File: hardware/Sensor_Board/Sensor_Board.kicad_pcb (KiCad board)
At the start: 2 copper layers, 83 x 83 mm, 55 parts, among them J1 Antenna, J2 Antenna, J3 Sensors, U1 ICM-42670-P, U10 PE42421, U12 SX1262IMLTRT, U2 SX1262IMLTRT, U3 0900FM15D0039, U4 BME280, U5 PE42421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

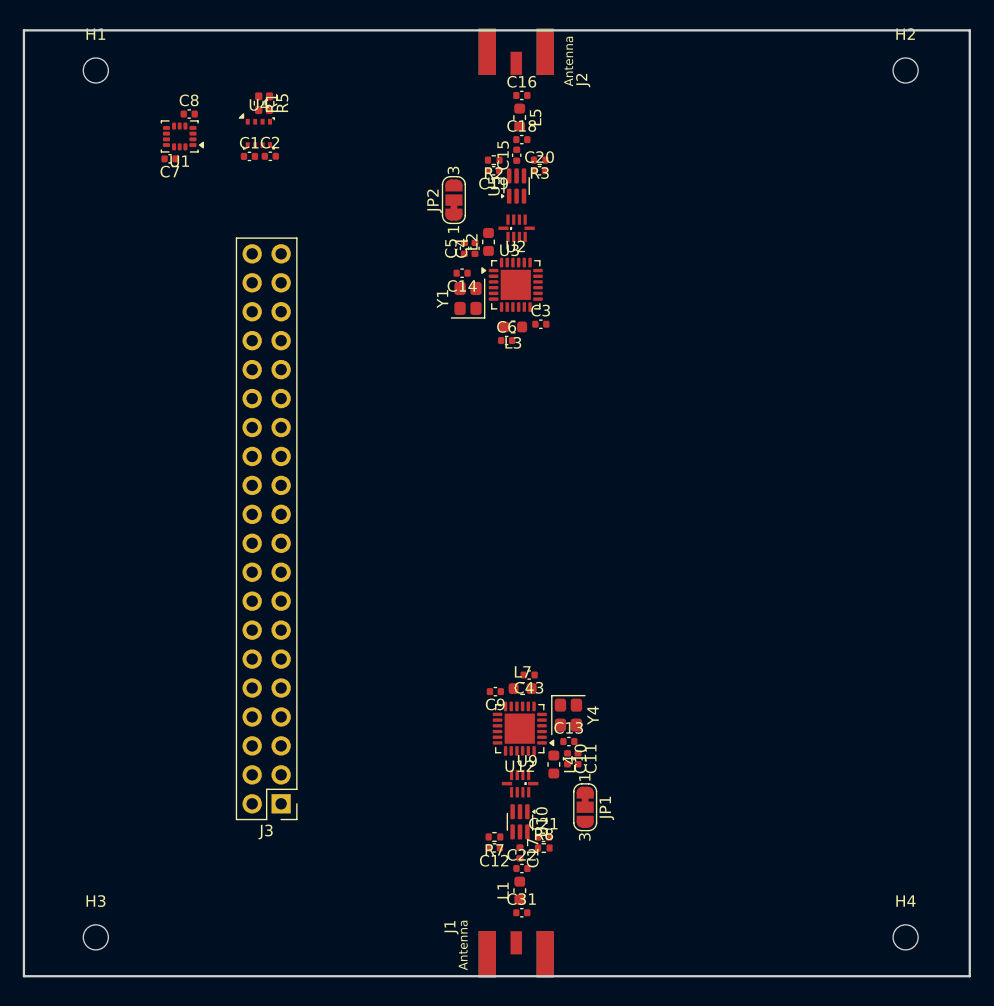
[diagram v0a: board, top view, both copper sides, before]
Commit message: feat(Hw):Update_Route_And_3d_Model_PWNsat_Batt_Board_And_Sensors
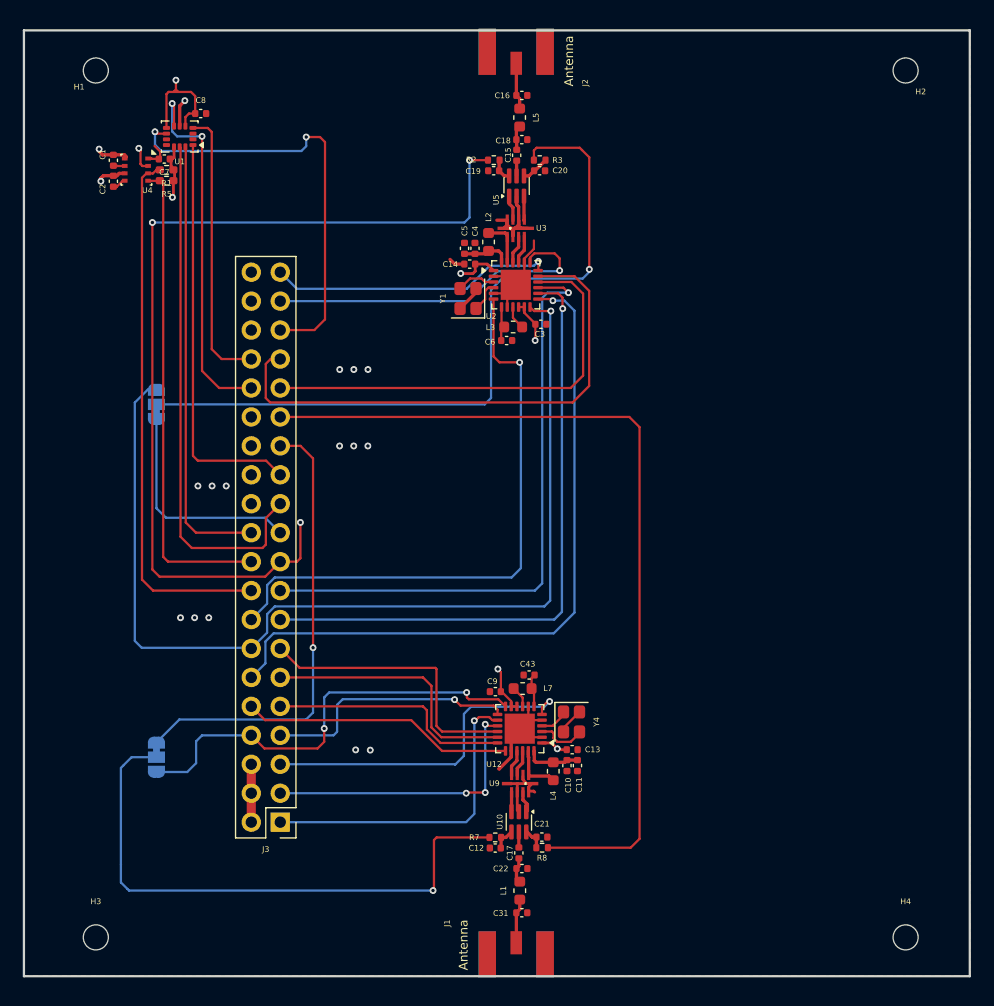
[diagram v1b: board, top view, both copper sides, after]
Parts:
- JP1, JP2: moved to B.Cu
- moved JP1 37.9 mm to (81.4, 122.4)
- moved JP2 31.7 mm to (81.4, 91.5)
- moved C2 13.9 mm to (77.7, 71.9), turned to -90 degrees
- moved C1 11.9 mm to (77.7, 70.1), turned to -90 degrees
- moved R5 11.3 mm to (82.3, 71.8), turned to 180 degrees
- moved U4 11.2 mm to (79.7, 70.9), turned to -90 degrees
- moved R1 9.98 mm to (82.3, 70.9), turned to 180 degrees
- moved J3 1.61 mm to (92.3, 128.1)
- moved C14 1.04 mm to (108.9, 79.2)
- moved C8 1.01 mm to (85.3, 66.0)
- moved C13 0.77 mm to (117.9, 121.8)
- moved Y4 0.66 mm to (117.8, 119.3)
- moved C10 0.60 mm to (117.5, 123.2)
- moved C11 0.60 mm to (118.4, 123.2)
- moved L4 0.60 mm to (116.2, 123.7)
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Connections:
- C13 pad 1: +3V3 -> +3.3V
- C14 pad 1: +3V3 -> +3.3V
- C3 pad 1: +3V3 -> +3.3V
- C9 pad 1: +3V3 -> +3.3V
- J3 pad 1: /Inputs_Connectors/DIO2 -> /Inputs_Connectors/R0_BUSY
- J3 pad 10: /Inputs_Connectors/SCL_ICM -> /Inputs_Connectors/R0_NSS
- J3 pad 11: /Inputs_Connectors/R0_RST -> /Inputs_Connectors/R0_MOSI
- J3 pad 12: /Inputs_Connectors/AP_ADO -> /Inputs_Connectors/R1_DIO1
- J3 pad 13: /Inputs_Connectors/R0_BUSY -> /Inputs_Connectors/R0_MISO
- J3 pad 14: /Inputs_Connectors/INT1 -> /Sensors/R1_DIO2
- J3 pad 15: /Inputs_Connectors/R0_DIO3 -> /Inputs_Connectors/R1_BUSY
- J3 pad 16: /Inputs_Connectors/FSYNC -> /Inputs_Connectors/R1_DIO3
- J3 pad 17: /Sensors/R0_DIO2 -> /Inputs_Connectors/R1_RST
- J3 pad 18: /Inputs_Connectors/INT2 -> /Inputs_Connectors/SDA_BME280
- J3 pad 19: /Inputs_Connectors/R0_DIO1 -> /Inputs_Connectors/R1_ANT_SW
- J3 pad 20: /Inputs_Connectors/SDA_BME280 -> /Inputs_Connectors/SCL_BME280
- J3 pad 21: /Inputs_Connectors/R0_ANT_SW -> /Inputs_Connectors/DIO23
- J3 pad 22: /Inputs_Connectors/SCL_BME280 -> /Inputs_Connectors/SDA_ICM
- J3 pad 23: /Inputs_Connectors/R1_ANT_SW -> /Inputs_Connectors/SCL_ICM
- J3 pad 25: /Inputs_Connectors/DIO23 -> /Inputs_Connectors/AP_ADO
- J3 pad 27: /Inputs_Connectors/R1_NSS -> /Inputs_Connectors/DIO2
- J3 pad 29: /Inputs_Connectors/R1_SCK -> /Inputs_Connectors/R0_ANT_SW
- J3 pad 3: /Inputs_Connectors/R0_NSS -> /Inputs_Connectors/R0_RST
- J3 pad 32: /Inputs_Connectors/R1_DIO1 -> /Inputs_Connectors/FSYNC
- J3 pad 34: /Sensors/R1_DIO2 -> /Inputs_Connectors/INT1
- J3 pad 35: /Inputs_Connectors/R1_RST -> /Inputs_Connectors/INT2
- J3 pad 37: /Inputs_Connectors/R1_BUSY -> /Inputs_Connectors/R1_NSS
- J3 pad 39: /Inputs_Connectors/R1_DIO3 -> /Inputs_Connectors/R1_SCK
- J3 pad 5: /Inputs_Connectors/R0_SCK -> /Inputs_Connectors/R0_DIO3
- J3 pad 7: /Inputs_Connectors/R0_MISO -> /Inputs_Connectors/R0_DIO1
- J3 pad 8: /Inputs_Connectors/SDA_ICM -> /Sensors/R0_DIO2
- J3 pad 9: /Inputs_Connectors/R0_MOSI -> /Inputs_Connectors/R0_SCK
- U12 pad 1: +3V3 -> +3.3V
- U12 pad 10: +3V3 -> +3.3V
- U12 pad 11: +3V3 -> +3.3V
- U2 pad 1: +3V3 -> +3.3V
- U2 pad 10: +3V3 -> +3.3V
- U2 pad 11: +3V3 -> +3.3V
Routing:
- net /Sensors/R1_DIO2: track 0.00 -> 90.1 mm, vias 0 -> 1
- net /Inputs_Connectors/R1_ANT_SW: track 0.00 -> 82.2 mm, vias 0 -> 3
- net /Inputs_Connectors/R0_ANT_SW: track 0.00 -> 76.4 mm
- net Net-(JP2-C): track 0.00 -> 64.6 mm, vias 0 -> 1
- net /Inputs_Connectors/R1_DIO1: track 0.00 -> 61.9 mm, vias 0 -> 1
- net /Inputs_Connectors/R1_BUSY: track 0.00 -> 54.9 mm, vias 0 -> 1
- net /Inputs_Connectors/R1_RST: track 0.00 -> 53.6 mm, vias 0 -> 1
- net /Inputs_Connectors/R1_DIO3: track 0.00 -> 52.1 mm, vias 0 -> 1
- net GND: track 0.00 -> 51.5 mm, vias 0 -> 15
- net Net-(JP1-C): track 0.00 -> 50.7 mm, vias 0 -> 1
- net /Inputs_Connectors/SDA_BME280: track 0.00 -> 47.1 mm
- net /Inputs_Connectors/R1_MOSI: track 0.00 -> 46.9 mm
- net /Inputs_Connectors/SCL_ICM: track 0.00 -> 46.4 mm
- net +3.3V: track 0.00 -> 42.8 mm, vias 0 -> 9
- net /Inputs_Connectors/SCL_BME280: track 0.00 -> 42.2 mm
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- added copper zone on In2.Cu, net +3.3V
- added copper zone on B.Cu, net GND
- added copper zone on F.Cu, net GND
- added copper zone on In1.Cu, net GND
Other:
- copper layers 2 -> 4

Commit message: fix(Hw):Tracks_modified
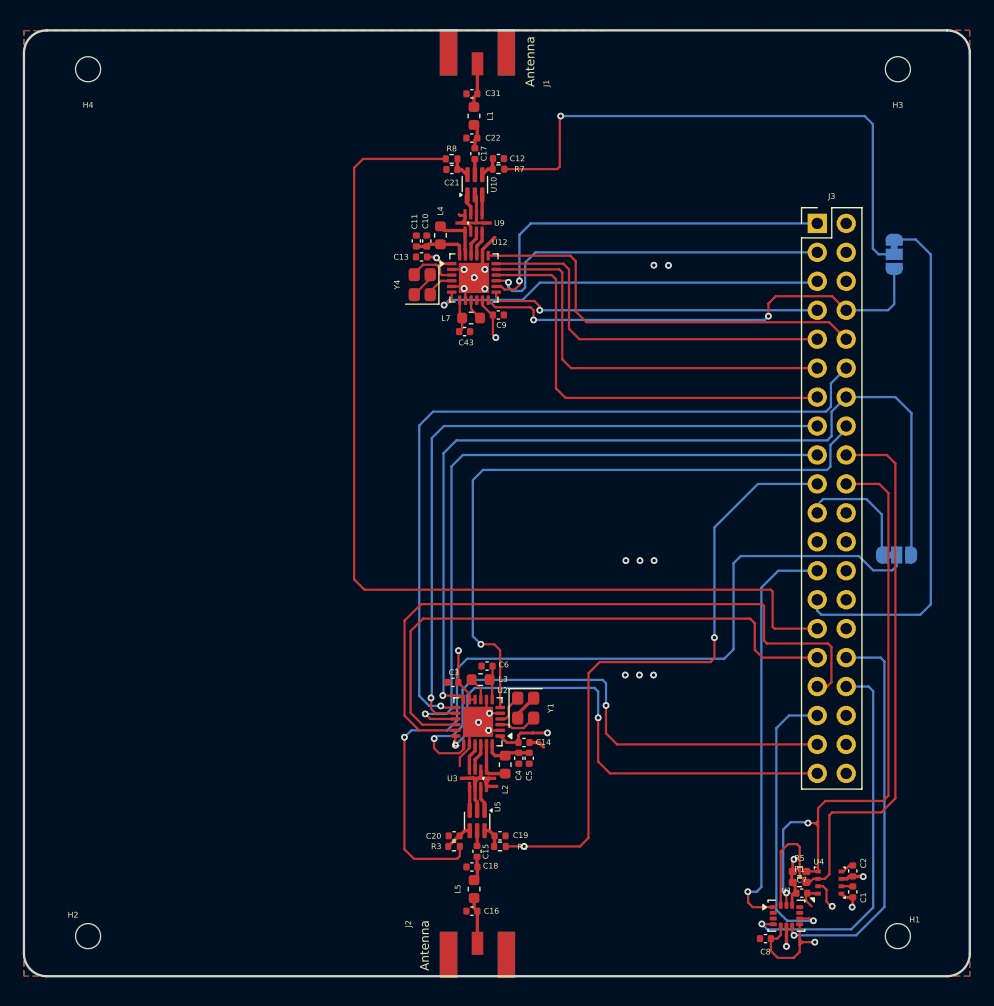
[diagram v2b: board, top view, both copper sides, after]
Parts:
- moved H4 104.6 mm to (75.4, 62.1), turned to 180 degrees
- moved H2 104.5 mm to (75.4, 138.1), turned to 180 degrees
- moved H3 103.7 mm to (146.5, 62.1), turned to 180 degrees
- moved H1 103.6 mm to (146.5, 138.1), turned to 180 degrees
- moved C1 91.3 mm to (142.5, 134.3), turned to 90 degrees
- moved C2 88.7 mm to (142.5, 132.4), turned to 90 degrees
- moved C8 87.7 mm to (134.9, 138.4), turned to 180 degrees
- moved U4 87.3 mm to (140.5, 133.4), turned to 90 degrees
- moved U1 86.7 mm to (136.7, 136.3), turned to 0 degrees
- moved C7 85.3 mm to (138.1, 134.4), turned to 0 degrees
- moved R1 83.6 mm to (137.9, 133.4), turned to 0 degrees
- moved J2 83.4 mm to (109.6, 141.8), turned to 90 degrees
- moved J1 83.3 mm to (109.6, 58.5), turned to -90 degrees
- moved R5 82.2 mm to (137.9, 132.5), turned to 0 degrees
- moved JP1 78.4 mm to (146.2, 78.3)
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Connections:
- J3 pad 18: /Inputs_Connectors/SDA_BME280 -> /Inputs_Connectors/SDA_SENS
- J3 pad 20: /Inputs_Connectors/SCL_BME280 -> /Inputs_Connectors/SCL_SENS
- J3 pad 22: /Inputs_Connectors/SDA_ICM -> unconnected-(J3-Pin_22-Pad22)
- J3 pad 23: /Inputs_Connectors/SCL_ICM -> unconnected-(J3-Pin_23-Pad23)
- R1 pad 2: /Inputs_Connectors/SDA_BME280 -> /Inputs_Connectors/SDA_SENS
- R5 pad 2: /Inputs_Connectors/SCL_BME280 -> /Inputs_Connectors/SCL_SENS
- U1 pad 13: /Inputs_Connectors/SCL_ICM -> /Inputs_Connectors/SCL_SENS
- U1 pad 14: /Inputs_Connectors/SDA_ICM -> /Inputs_Connectors/SDA_SENS
- U4 pad 3: /Inputs_Connectors/SDA_BME280 -> /Inputs_Connectors/SDA_SENS
- U4 pad 4: /Inputs_Connectors/SCL_BME280 -> /Inputs_Connectors/SCL_SENS
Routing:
- net /Inputs_Connectors/SDA_SENS: track 0.00 -> 58.0 mm
- net /Inputs_Connectors/SCL_SENS: track 0.00 -> 54.4 mm, vias 0 -> 2
- net /Inputs_Connectors/SDA_BME280: track 47.1 -> 0.00 mm
- net /Inputs_Connectors/SCL_ICM: track 46.4 -> 0.00 mm
- net /Inputs_Connectors/SCL_BME280: track 42.2 -> 0.00 mm
- net /Inputs_Connectors/SDA_ICM: track 39.1 -> 0.00 mm
- net /Inputs_Connectors/R1_ANT_SW: track 82.2 -> 55.7 mm, vias 3 -> 2
- net /Inputs_Connectors/R1_SCK: track 25.1 -> 43.3 mm, vias 1 -> 2
- net /Inputs_Connectors/R1_NSS: track 30.1 -> 46.8 mm, vias 1 -> 2
- net /Inputs_Connectors/INT2: track 38.4 -> 24.9 mm, vias 2 -> 1
- net /Inputs_Connectors/R0_MISO: track 25.0 -> 38.3 mm
- net /Inputs_Connectors/R0_NSS: track 23.9 -> 37.0 mm
- net /Inputs_Connectors/R0_MOSI: track 23.4 -> 36.2 mm
- net /Inputs_Connectors/R0_SCK: track 21.4 -> 34.0 mm
- net /Inputs_Connectors/R0_ANT_SW: track 76.4 -> 88.7 mm
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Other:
- outline, holes or cut-outs redrawn

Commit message: feat(Hw):Labels_Added
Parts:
- added G***: LOGO, LOGO, F.Cu at (145.9, 133.2)
- added G***: LOGO, LOGO, F.Cu at (132.1, 136.5)
- added G***: LOGO, Aesthetics:electronic_cats_logo_8x6, F.Cu at (109.6, 98.5)
- added G***: LOGO, Aesthetics:electronic_cats_logo_8x6, B.Cu at (126.4, 96.2)
- added REF**: OSHW-Logo_5.7x6mm_SilkScreen, Symbol:OSHW-Logo_5.7x6mm_SilkScreen, B.Cu at (92.7, 96.3)
- added kibuzzard-698518BF: G***, kibuzzard-698518BF, F.Cu at (109.8, 91.6)
- added kibuzzard-698518BF: G***, kibuzzard-698518BF, B.Cu at (110.4, 88.2)
- added kibuzzard-698518EC: G***, kibuzzard-698518EC, F.Cu at (109.6, 107.9)
- added kibuzzard-698518EC: G***, kibuzzard-698518EC, B.Cu at (109.9, 104.3)
- added kibuzzard-6985197E: G***, kibuzzard-6985197E, F.Cu at (132.9, 99.4)

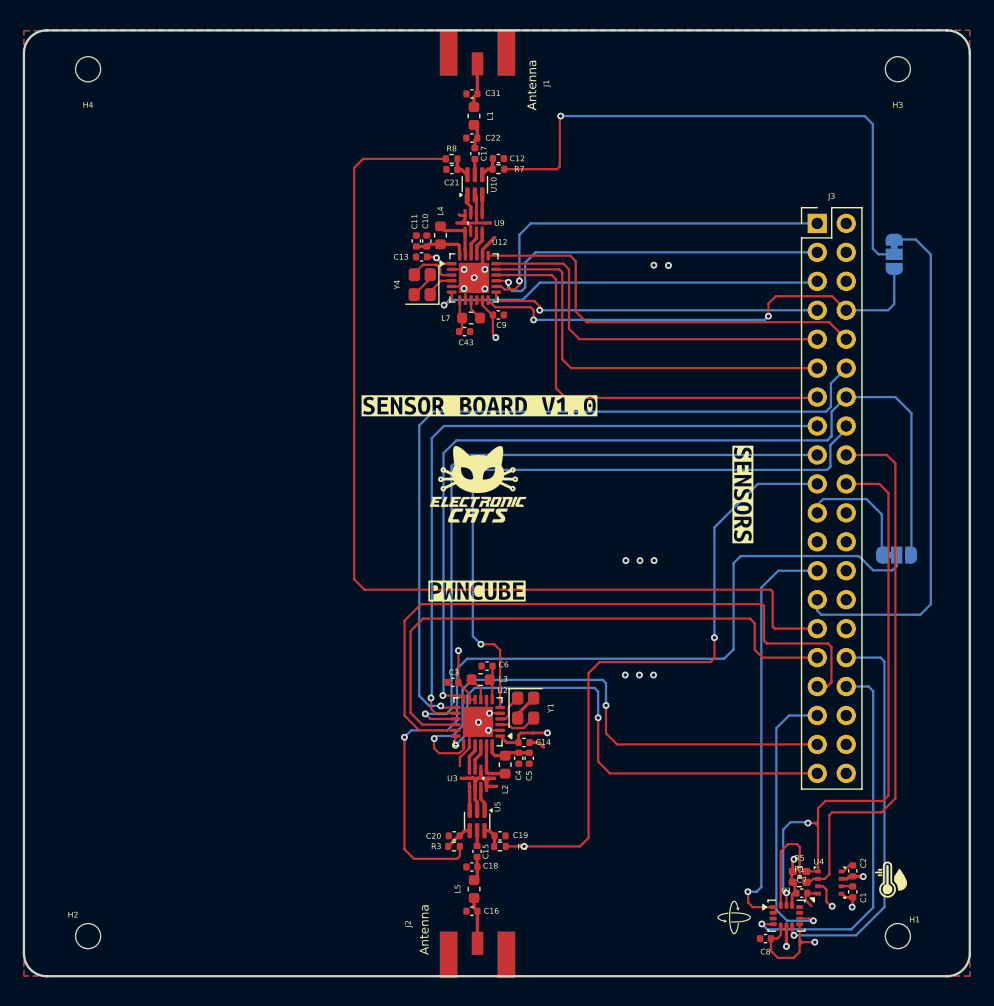
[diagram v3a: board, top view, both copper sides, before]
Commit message: feat(Hw):Update_Labels
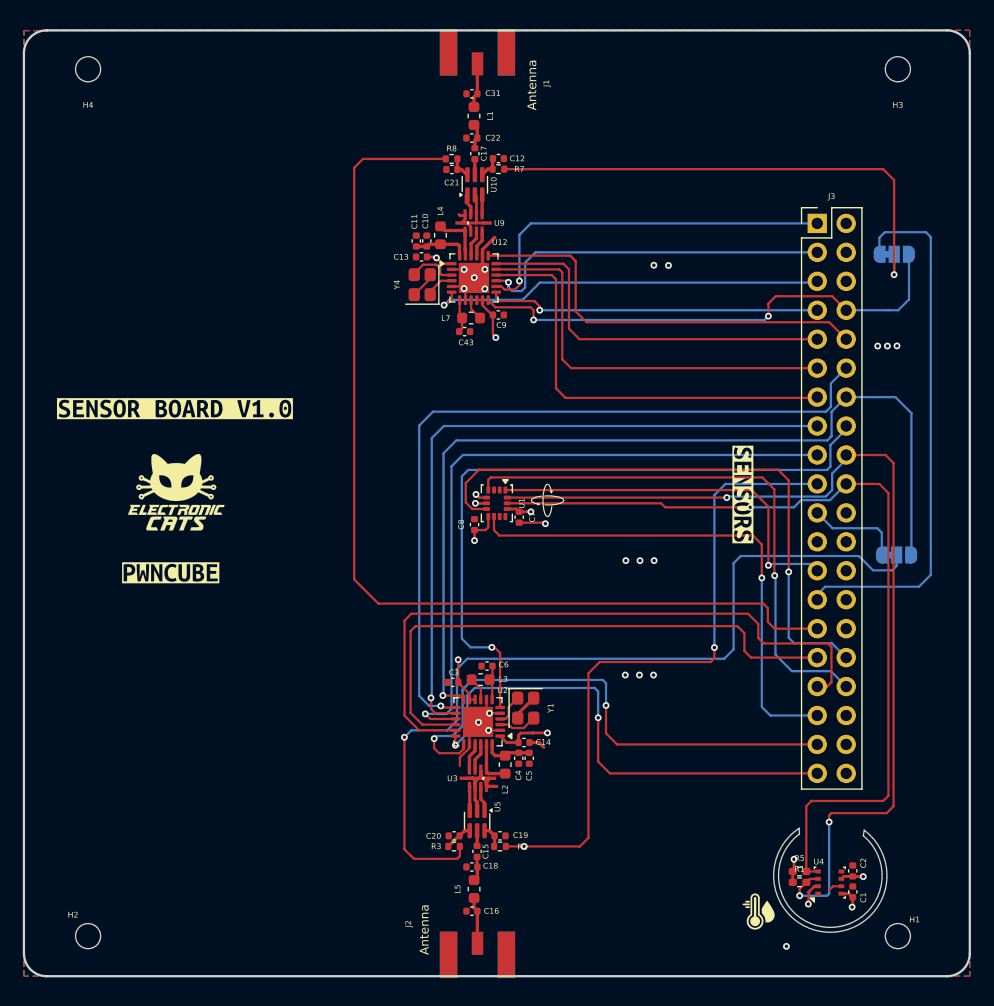
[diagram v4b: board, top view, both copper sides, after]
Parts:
- added kibuzzard-69860F52: G***, kibuzzard-69860F52, B.Cu at (150.5, 104.5)
- added kibuzzard-69860F65: G***, kibuzzard-69860F65, B.Cu at (150.5, 78.6)
- moved C8 44.4 mm to (109.3, 102.0), turned to 90 degrees
- moved U1 44.2 mm to (111.3, 100.2), turned to -90 degrees
- moved C7 41.3 mm to (113.3, 101.4), turned to -90 degrees
- moved G*** 40.1 mm to (115.7, 99.9)
- moved kibuzzard-698518EC 26.9 mm to (82.7, 106.3)
- moved kibuzzard-698518BF 26.7 mm to (83.1, 91.9)
- moved G*** 26.5 mm to (83.2, 99.2)
- moved G*** 12.0 mm to (134.3, 136.0)
- turned JP1 to 0 degrees
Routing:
- net /Inputs_Connectors/SDA_SENS: track 58.0 -> 85.0 mm, vias 0 -> 3
- net /Inputs_Connectors/SCL_SENS: track 54.4 -> 75.7 mm, vias 2 -> 1
- net /Inputs_Connectors/INT2: track 24.9 -> 44.7 mm
- net /Inputs_Connectors/FSYNC: track 34.9 -> 52.5 mm
- net /Inputs_Connectors/INT1: track 33.3 -> 48.4 mm
- net +3.3V: track 38.6 -> 30.8 mm, vias 9 -> 11
- net Net-(JP1-C): track 50.1 -> 44.7 mm
- net /Inputs_Connectors/AP_ADO: track 36.5 -> 33.4 mm
- net /Sensors/R0_DIO2: track 42.2 -> 44.5 mm
- net /Inputs_Connectors/DIO23: track 10.7 -> 8.35 mm
- net /Inputs_Connectors/R1_DIO3: track 57.6 -> 59.7 mm
- net /Inputs_Connectors/R1_MOSI: track 59.3 -> 57.5 mm
- net /Inputs_Connectors/R1_ANT_SW: track 55.7 -> 57.4 mm
- net /Inputs_Connectors/DIO2: track 45.9 -> 47.1 mm
- net /Inputs_Connectors/R0_ANT_SW: track 88.7 -> 87.6 mm
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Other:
- outline, holes or cut-outs redrawn

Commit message: feat(Hw):BME280_Moved
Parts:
- moved R5 15.3 mm to (123.1, 128.3)
- moved R1 15.3 mm to (123.1, 129.2)
- moved C1 15.3 mm to (127.8, 130.1)
- moved C2 15.3 mm to (127.8, 128.2)
- moved U4 15.3 mm to (125.8, 129.3)
- moved G*** 13.7 mm to (126.2, 124.9)
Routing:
- net /Inputs_Connectors/SCL_SENS: track 75.7 -> 91.1 mm
- net /Inputs_Connectors/SDA_SENS: track 85.0 -> 97.0 mm, vias 3 -> 1
- net +3.3V: track 30.8 -> 35.0 mm, vias 11 -> 9
- net GND: track 50.1 -> 54.2 mm, vias 22 -> 24
- net /Inputs_Connectors/R1_SCK: track 43.3 -> 42.8 mm
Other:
- outline, holes or cut-outs redrawn
